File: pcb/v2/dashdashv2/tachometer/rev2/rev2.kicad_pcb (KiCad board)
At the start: 2 copper layers, 113 parts, among them Q1 BSS138, Q2 BSS138, Q3 BSS138, Q4 BSS138, Q5 BSS138

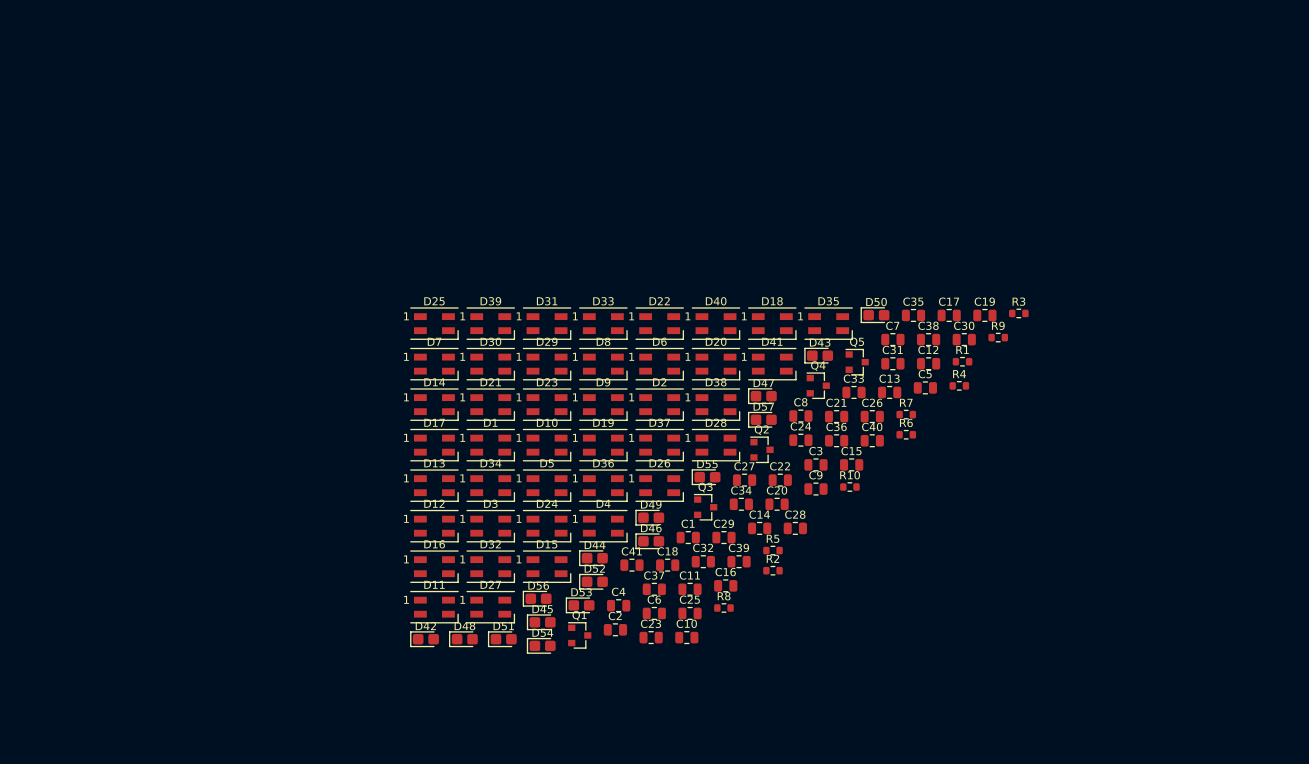
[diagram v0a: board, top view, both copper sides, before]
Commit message: tachometer, add neopixels
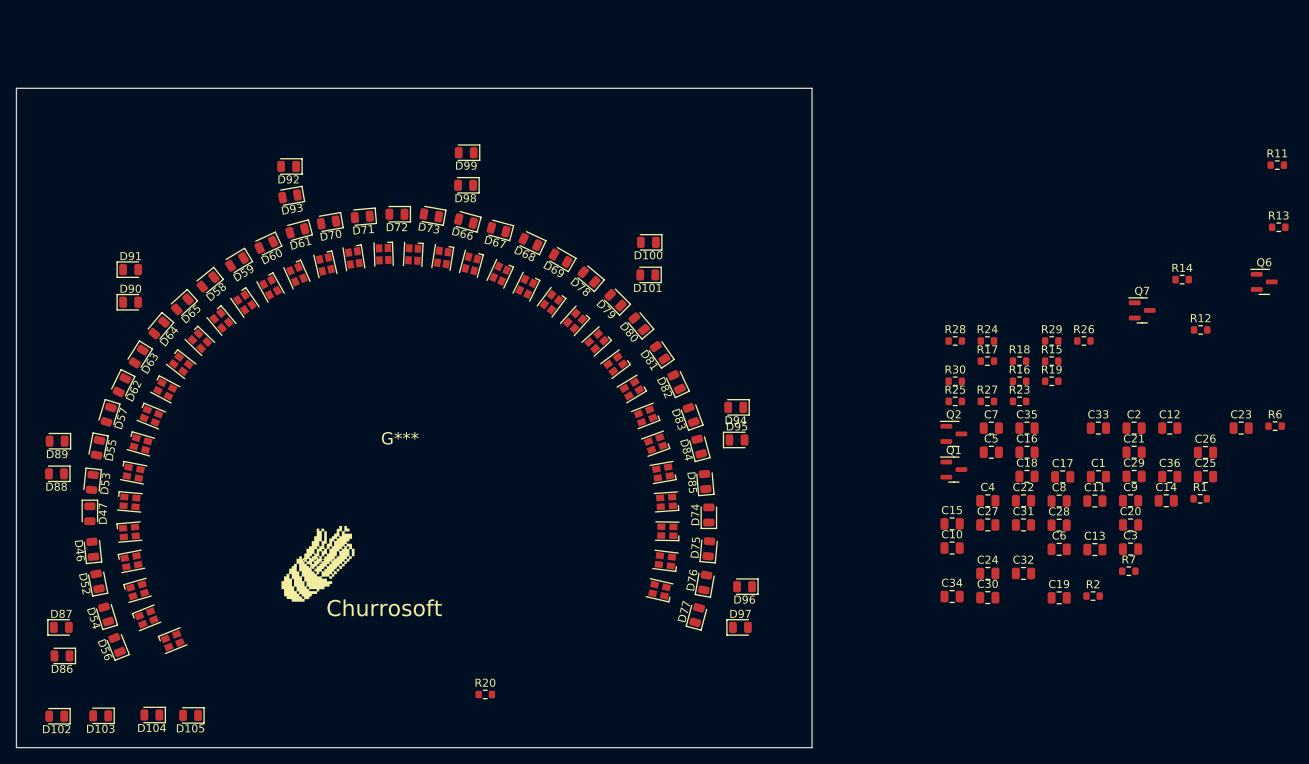
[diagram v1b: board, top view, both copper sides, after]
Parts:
- removed C37, C38, C39, C40, C41: 100nF, Capacitor_SMD:C_0805_2012Metric
- removed D37, D38, D39, D40, D41: WS2812B, LED_SMD:LED_SK6812MINI_PLCC4_3.5x3.5mm_P1.75mm
- removed D42, D43, D44, D45, D48, D49, D50, D51: LED, LED_SMD:LED_0805_2012Metric_Castellated
- removed Q3, Q4, Q5: BSS138, Package_TO_SOT_SMD:SOT-23
- removed R10, R3, R4, R5, R8, R9: 1k 1/10W +-1%, Resistor_SMD:R_0603_1608Metric
- added D100: LED, LED_SMD:LED_0805_2012Metric, F.Cu at (148.8, 78.1)
- added D101: LED, LED_SMD:LED_0805_2012Metric, F.Cu at (148.7, 82.2)
- added D102: LED, LED_SMD:LED_0805_2012Metric, F.Cu at (75.1, 137.2)
- added D103: LED, LED_SMD:LED_0805_2012Metric, F.Cu at (80.5, 137.2)
- added D104: LED, LED_SMD:LED_0805_2012Metric, F.Cu at (86.9, 137.1)
- added D105: LED, LED_SMD:LED_0805_2012Metric, F.Cu at (91.7, 137.1)
- added D58: LED, LED_SMD:LED_0805_2012Metric, F.Cu at (93.9, 83.1)
- added D59: LED, LED_SMD:LED_0805_2012Metric, F.Cu at (97.5, 80.6)
- added D60: LED, LED_SMD:LED_0805_2012Metric, F.Cu at (101.2, 78.4)
- added D61: LED, LED_SMD:LED_0805_2012Metric, F.Cu at (105.1, 76.7)
- added D62: LED, LED_SMD:LED_0805_2012Metric, F.Cu at (83.2, 95.9)
- added D63: LED, LED_SMD:LED_0805_2012Metric, F.Cu at (85.3, 92.4)
- added D64: LED, LED_SMD:LED_0805_2012Metric, F.Cu at (87.8, 88.8)
- added D65: LED, LED_SMD:LED_0805_2012Metric, F.Cu at (90.7, 85.9)
- added D66: LED, LED_SMD:LED_0805_2012Metric, F.Cu at (126.1, 75.5)
- added D67: LED, LED_SMD:LED_0805_2012Metric, F.Cu at (130.1, 76.6)
- added D68: LED, LED_SMD:LED_0805_2012Metric, F.Cu at (134.1, 78.1)
- added D69: LED, LED_SMD:LED_0805_2012Metric, F.Cu at (137.9, 80.1)
- added D70: LED, LED_SMD:LED_0805_2012Metric, F.Cu at (109.0, 75.7)
- added D71: LED, LED_SMD:LED_0805_2012Metric, F.Cu at (113.2, 75.0)
- added D72: LED, LED_SMD:LED_0805_2012Metric, F.Cu at (117.5, 74.6)
- added D73: LED, LED_SMD:LED_0805_2012Metric, F.Cu at (121.8, 74.8)
- added D74: LED, LED_SMD:LED_0805_2012Metric, F.Cu at (156.4, 112.1)
- added D75: LED, LED_SMD:LED_0805_2012Metric, F.Cu at (156.4, 116.3)
- added D76: LED, LED_SMD:LED_0805_2012Metric, F.Cu at (155.9, 120.5)
- added D77: LED, LED_SMD:LED_0805_2012Metric, F.Cu at (154.9, 124.6)
- added D78: LED, LED_SMD:LED_0805_2012Metric, F.Cu at (141.4, 82.5)
- added D79: LED, LED_SMD:LED_0805_2012Metric, F.Cu at (144.7, 85.3)
- added D80: LED, LED_SMD:LED_0805_2012Metric, F.Cu at (147.7, 88.3)
- added D81: LED, LED_SMD:LED_0805_2012Metric, F.Cu at (150.3, 91.9)
- added D82: LED, LED_SMD:LED_0805_2012Metric, F.Cu at (152.3, 95.6)
- added D83: LED, LED_SMD:LED_0805_2012Metric, F.Cu at (154.2, 99.7)
- added D84: LED, LED_SMD:LED_0805_2012Metric, F.Cu at (155.2, 103.6)
- added D85: LED, LED_SMD:LED_0805_2012Metric, F.Cu at (155.9, 108.0)
- added D86: LED, LED_SMD:LED_0805_2012Metric, F.Cu at (75.7, 129.7)
- added D87: LED, LED_SMD:LED_0805_2012Metric, F.Cu at (75.6, 126.1)
- added D88: LED, LED_SMD:LED_0805_2012Metric, F.Cu at (75.0, 107.0)
- added D89: LED, LED_SMD:LED_0805_2012Metric, F.Cu at (75.1, 102.9)
- added D90: LED, LED_SMD:LED_0805_2012Metric, F.Cu at (84.3, 85.6)
- added D91: LED, LED_SMD:LED_0805_2012Metric, F.Cu at (84.3, 81.5)
- added D92: LED, LED_SMD:LED_0805_2012Metric, F.Cu at (104.0, 68.7)
- added D93: LED, LED_SMD:LED_0805_2012Metric, F.Cu at (104.1, 72.4)
- added D94: LED, LED_SMD:LED_0805_2012Metric, F.Cu at (159.7, 98.7)
- added D95: LED, LED_SMD:LED_0805_2012Metric, F.Cu at (159.9, 102.8)
- added D96: LED, LED_SMD:LED_0805_2012Metric, F.Cu at (160.8, 121.1)
- added D97: LED, LED_SMD:LED_0805_2012Metric, F.Cu at (160.3, 126.1)
- added D98: LED, LED_SMD:LED_0805_2012Metric, F.Cu at (126.0, 71.0)
- added D99: LED, LED_SMD:LED_0805_2012Metric, F.Cu at (126.1, 67.0)
- added G***: LOGO, LOGO, F.Cu at (117.9, 102.6)
- added G***: LOGO, LOGO, F.Cu at (107.8, 118.2)
- added Q6: BSS138, Package_TO_SOT_SMD:SOT-23, F.Cu at (225.6, 83.1)
- added Q7: BSS138, Package_TO_SOT_SMD:SOT-23, F.Cu at (210.4, 86.6)
- added R11: 1k 1/10W +-1%, Resistor_SMD:R_0603_1608Metric, F.Cu at (227.2, 68.5)
- added R12: 1k 1/10W +-1%, Resistor_SMD:R_0603_1608Metric, F.Cu at (217.7, 89.1)
- added R13: 1k 1/10W +-1%, Resistor_SMD:R_0603_1608Metric, F.Cu at (227.4, 76.3)
- added R14: 1k 1/10W +-1%, Resistor_SMD:R_0603_1608Metric, F.Cu at (215.4, 82.8)
- added R15: 1k 1/10W +-1%, Resistor_SMD:R_0603_1608Metric, F.Cu at (199.1, 92.9)
- added R16: 1k 1/10W +-1%, Resistor_SMD:R_0603_1608Metric, F.Cu at (195.1, 95.4)
- added R17: 1k 1/10W +-1%, Resistor_SMD:R_0603_1608Metric, F.Cu at (191.1, 92.9)
- added R18: 1k 1/10W +-1%, Resistor_SMD:R_0603_1608Metric, F.Cu at (195.1, 92.9)
- added R19: 1k 1/10W +-1%, Resistor_SMD:R_0603_1608Metric, F.Cu at (199.1, 95.4)
- added R20: 1k 1/10W +-1%, Resistor_SMD:R_0603_1608Metric, F.Cu at (128.5, 134.5)
- added R23: 1k 1/10W +-1%, Resistor_SMD:R_0603_1608Metric, F.Cu at (195.1, 98.0)
- added R24: 1k 1/10W +-1%, Resistor_SMD:R_0603_1608Metric, F.Cu at (191.1, 90.4)
- added R25: 1k 1/10W +-1%, Resistor_SMD:R_0603_1608Metric, F.Cu at (187.1, 98.0)
- added R26: 1k 1/10W +-1%, Resistor_SMD:R_0603_1608Metric, F.Cu at (203.1, 90.4)
- added R27: 1k 1/10W +-1%, Resistor_SMD:R_0603_1608Metric, F.Cu at (191.1, 98.0)
- added R28: 1k 1/10W +-1%, Resistor_SMD:R_0603_1608Metric, F.Cu at (187.1, 90.4)
- added R29: 1k 1/10W +-1%, Resistor_SMD:R_0603_1608Metric, F.Cu at (199.1, 90.4)
- added R30: 1k 1/10W +-1%, Resistor_SMD:R_0603_1608Metric, F.Cu at (187.1, 95.4)
- D1, D10, D11, D12, D13, D14, D15, D16, D17, D18, D19, D2, D20, D21, D22, D23, D24, D25, D26, D27, D28, D29, D3, D30, D31, D32, D33, D34, D35, D36, D4, D5, D6, D7, D8, D9: footprint LED_SMD:LED_SK6812MINI_PLCC4_3.5x3.5mm_P1.75mm -> LED_SMD:LED_Cree-PLCC4_2x2mm_CW
- D46, D47, D52, D53, D54, D55, D56, D57: footprint LED_SMD:LED_0805_2012Metric_Castellated -> LED_SMD:LED_0805_2012Metric
- moved D47 85.3 mm to (79.2, 112.0), turned to -90 degrees
- moved D57 81.7 mm to (81.5, 99.6), turned to -107 degrees
- moved C23 78.1 mm to (222.7, 101.3)
- moved D55 76.1 mm to (80.2, 103.7), turned to -101 degrees
- moved D46 69.6 mm to (79.5, 116.4), turned to 96 degrees
- moved C2 69.4 mm to (209.4, 101.3)
- moved D2 69.3 mm to (86.3, 124.9), turned to 22 degrees
- moved D6 68.2 mm to (84.2, 110.5), turned to -5 degrees
- moved C25 66.5 mm to (218.3, 107.3)
- moved D53 62.9 mm to (79.5, 108.1), turned to -96 degrees
- moved D52 62.0 mm to (80.2, 120.4), turned to 101 degrees
- moved D4 59.0 mm to (84.4, 117.9), turned to 11 degrees
- moved D8 58.5 mm to (85.6, 103.3), turned to -16 degrees
- moved D9 56.4 mm to (86.9, 99.8), turned to -22 degrees
- moved D54 54.5 mm to (81.2, 124.5), turned to 107 degrees
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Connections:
- D56 pad 1: /BA_1 -> Net-(D56-Pad1)
- D57 pad 1: /BA_2 -> Net-(D57-Pad1)
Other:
- board outline added: 99.2 x 82.2 mm
- board text added: "Churrosoft"

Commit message: routing neopixel
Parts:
- moved D1 1.91 mm to (87.8, 128.5)
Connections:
- C27 pad 2: Net-(C27-Pad2) -> +5VA
- C28 pad 2: Net-(C27-Pad2) -> +5VA
- C29 pad 2: Net-(C27-Pad2) -> +5VA
- C30 pad 2: Net-(C27-Pad2) -> +5VA
- C31 pad 2: Net-(C27-Pad2) -> +5VA
- D27 pad 1: Net-(C27-Pad2) -> +5VA
- D28 pad 1: Net-(C27-Pad2) -> +5VA
- D29 pad 1: Net-(C27-Pad2) -> +5VA
- D30 pad 1: Net-(C27-Pad2) -> +5VA
- D31 pad 1: Net-(C27-Pad2) -> +5VA
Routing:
- net Net-(D16-Pad2): track 0.00 -> 3.78 mm
- net Net-(D17-Pad2): track 0.00 -> 3.74 mm
- net Net-(D10-Pad2): track 0.00 -> 3.72 mm
- net Net-(D18-Pad2): track 0.00 -> 3.72 mm
- net Net-(D12-Pad2): track 0.00 -> 3.67 mm
- net Net-(D11-Pad2): track 0.00 -> 3.66 mm
- net Net-(D23-Pad2): track 0.00 -> 3.62 mm
- net Net-(D15-Pad2): track 0.00 -> 3.58 mm
- net Net-(D10-Pad4): track 0.00 -> 3.49 mm
- net Net-(D4-Pad2): track 0.00 -> 3.45 mm
- net Net-(D29-Pad2): track 0.00 -> 3.41 mm
- net Net-(D3-Pad2): track 0.00 -> 3.39 mm
- net Net-(D8-Pad2): track 0.00 -> 3.35 mm
- net Net-(D22-Pad2): track 0.00 -> 3.29 mm
- net Net-(D1-Pad2): track 0.00 -> 3.27 mm
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
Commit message: tach v2, routing & 3D
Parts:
- removed R12, R13, R2, R6: 1k 1/10W +-1%, Resistor_SMD:R_0603_1608Metric
- added C37: 100nF, Capacitor_SMD:C_0805_2012Metric, B.Cu at (169.7, 73.8)
- added C38: 100nF, Capacitor_SMD:C_0805_2012Metric, B.Cu at (172.2, 76.4)
- added C39: 100nF, Capacitor_SMD:C_0805_2012Metric, B.Cu at (174.6, 79.2)
- added C40: 100nF, Capacitor_SMD:C_0805_2012Metric, B.Cu at (176.6, 82.6)
- added C41: 100nF, Capacitor_SMD:C_0805_2012Metric, B.Cu at (178.3, 85.9)
- added C42: 100nF, Capacitor_SMD:C_0805_2012Metric, B.Cu at (179.5, 89.4)
- added C43: 100nF, Capacitor_SMD:C_0805_2012Metric, B.Cu at (180.4, 92.9)
- added C44: 100nF, Capacitor_SMD:C_0805_2012Metric, B.Cu at (180.7, 96.4)
- added C45: 100nF, Capacitor_SMD:C_0805_2012Metric, B.Cu at (180.8, 100.2)
- added C46: 100nF, Capacitor_SMD:C_0805_2012Metric, B.Cu at (180.5, 103.8)
- added C47: 100nF, Capacitor_SMD:C_0805_2012Metric, B.Cu at (179.7, 107.6)
- added C53: 100nF, Capacitor_SMD:C_0603_1608Metric, B.Cu at (155.3, 106.8)
- added C54: 30pF, Capacitor_SMD:C_0603_1608Metric, B.Cu at (136.7, 95.1)
- added C55: 30pF, Capacitor_SMD:C_0603_1608Metric, B.Cu at (136.7, 87.8)
- added C56: 100nF, Capacitor_SMD:C_0603_1608Metric, B.Cu at (162.7, 113.4)
- added C57: 30pF, Capacitor_SMD:C_0603_1608Metric, B.Cu at (161.4, 117.0)
- added C58: 2.2uF, Capacitor_SMD:C_0603_1608Metric, B.Cu at (147.1, 98.4)
- added D106: GREEN, LED_SMD:LED_0603_1608Metric, B.Cu at (192.4, 68.5)
- added D107: BLUE, LED_SMD:LED_0603_1608Metric, B.Cu at (189.9, 74.0)
- added D108: RED, LED_SMD:LED_0603_1608Metric, B.Cu at (185.6, 72.2)
- added D111: WS2812B, LED_SMD:LED_Cree-PLCC4_2x2mm_CW, F.Cu at (119.5, 109.3)
- added D112: WS2812B, LED_SMD:LED_Cree-PLCC4_2x2mm_CW, F.Cu at (118.5, 106.3)
- added D113: WS2812B, LED_SMD:LED_Cree-PLCC4_2x2mm_CW, F.Cu at (117.9, 103.0)
- added D114: WS2812B, LED_SMD:LED_Cree-PLCC4_2x2mm_CW, F.Cu at (117.7, 99.7)
- added D115: WS2812B, LED_SMD:LED_Cree-PLCC4_2x2mm_CW, F.Cu at (117.8, 96.5)
- added H1: MountingHole, MountingHole:MountingHole_2.2mm_M2_Pad, F.Cu at (110.0, 60.0)
- added H10: USB+, TestPoint:TestPoint_Pad_D1.5mm, B.Cu at (152.8, 76.8)
- added H11: USB_GND, TestPoint:TestPoint_Pad_D1.5mm, B.Cu at (167.0, 88.3)
- added H2: MountingHole, MountingHole:MountingHole_2.2mm_M2_Pad, F.Cu at (125.0, 115.0)
- added H3: MountingHole, MountingHole:MountingHole_2.2mm_M2_Pad, F.Cu at (165.3, 82.4)
- added H4: MountingHole, MountingHole:MountingHole_2.2mm_M2_Pad, F.Cu at (169.2, 61.1)
- added H5: MountingHole, MountingHole:MountingHole_2.2mm_M2_Pad, F.Cu at (131.1, 61.6)
- added H6: MountingHole, MountingHole:MountingHole_2.2mm_M2_Pad, F.Cu at (185.0, 60.0)
- added H7: MountingHole, MountingHole:MountingHole_2.2mm_M2_Pad, F.Cu at (180.0, 115.0)
- added H8: MountingHole, MountingHole:MountingHole_2.2mm_M2_Pad, F.Cu at (133.0, 80.0)
- added H9: USB-, TestPoint:TestPoint_Pad_D1.5mm, B.Cu at (158.7, 77.3)
- added J1: Tag connect, Connector:Tag-Connect_TC2030-IDC-FP_2x03_P1.27mm_Vertical, B.Cu at (159.1, 89.0)
- added J2: RPM_CONN1, Connector_PinHeader_1.27mm:PinHeader_2x05_P1.27mm_Vertical, B.Cu at (126.9, 94.5)
- added JP1: BOOTSEL, Jumper:SolderJumper-2_P1.3mm_Open_TrianglePad1.0x1.5mm, B.Cu at (142.2, 79.1)
- added R21: 10k, Resistor_SMD:R_0603_1608Metric, B.Cu at (151.3, 83.0)
- added R22: 1k, Resistor_SMD:R_0603_1608Metric, B.Cu at (140.7, 82.4)
- added R31: 1k, Resistor_SMD:R_0603_1608Metric, B.Cu at (189.2, 68.4)
- added R32: 27R, Resistor_SMD:R_0603_1608Metric, B.Cu at (153.8, 80.1)
- added R33: 27R, Resistor_SMD:R_0603_1608Metric, B.Cu at (157.0, 80.6)
- added R34: 1k, Resistor_SMD:R_0603_1608Metric, B.Cu at (193.6, 73.2)
- added R35: 1k, Resistor_SMD:R_0603_1608Metric, B.Cu at (185.9, 67.9)
- added U1: W25Q128JVS, Package_SO:SOIC-8_5.23x5.23mm_P1.27mm, B.Cu at (146.5, 78.0)
- added U2: LP5907MFX-3.3, Package_TO_SOT_SMD:SOT-23-5, B.Cu at (131.0, 110.5)
- added U3: SRV05-4, Package_TO_SOT_SMD:SOT-23-6, B.Cu at (133.4, 97.5)
- added U4: RP2040, Package_DFN_QFN:QFN-56-1EP_7x7mm_P0.4mm_EP3.2x3.2mm, B.Cu at (146.1, 92.0)
- added U6: YAAJ_DCDC_StepDown_LM2596, dashdash_lib:YAAJ_DCDC_StepDown_LM2596, B.Cu at (171.2, 105.7)
- added Y1: 12MHz, Crystal:Crystal_SMD_3225-4Pin_3.2x2.5mm, B.Cu at (136.6, 91.6)
- C1: value 100nF -> 2.2uF; footprint Capacitor_SMD:C_0805_2012Metric -> Capacitor_SMD:C_0603_1608Metric; moved to B.Cu
- C10, C11, C2, C3, C4, C5, C6, C7, C8, C9: footprint Capacitor_SMD:C_0805_2012Metric -> Capacitor_SMD:C_0603_1608Metric; moved to B.Cu
- C12, C13, C14, C15, C16, C17, C18, C19, C20, C21, C22, C23, C24, C25, C26, C27, C28, C29, C30, C31, C32, C33, C34, C35, C36, Q1, Q2, Q6, Q7, R1, R11, R14, R15, R16, R17, R18, R19, R20, R23, R24, R25, R26, R27, R28, R29, R30, R7: moved to B.Cu
- moved R7 103.7 mm to (115.2, 74.5)
- moved C23 102.9 mm to (122.9, 76.1), turned to 130 degrees
- moved C14 98.4 mm to (115.0, 107.2), turned to -170 degrees
- moved C12 97.1 mm to (117.6, 114.0), turned to -160 degrees
- moved C25 96.7 mm to (128.5, 71.3), turned to 110 degrees
- moved C20 96.4 mm to (116.6, 85.5), turned to 160 degrees
- moved C21 93.7 mm to (118.3, 82.1), turned to 150 degrees
- moved C26 93.4 mm to (131.6, 69.5), turned to 100 degrees
- moved C19 91.0 mm to (115.4, 89.0), turned to 160 degrees
- moved R16 90.5 mm to (105.0, 86.5), turned to 180 degrees
- moved R29 90.5 mm to (109.3, 101.9), turned to -90 degrees
- moved R1 90.0 mm to (144.6, 57.6), turned to 90 degrees
- moved C13 88.6 mm to (116.1, 110.6), turned to -160 degrees
- moved C17 87.1 mm to (114.1, 96.2), turned to 170 degrees
- moved C18 82.8 mm to (114.6, 92.5), turned to 160 degrees
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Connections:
- net +12V renamed +12LF
- net /DIN renamed /TACH_DIN
- C1 pad 2: +5VA -> +3V3
- C10 pad 1: GND -> +1V1
- C10 pad 2: +5VA -> GND
- C11 pad 1: GND -> +1V1
- C11 pad 2: +5VA -> GND
- C2 pad 1: GND -> +3V3
- C2 pad 2: +5VA -> GND
- C3 pad 1: GND -> +3V3
- C3 pad 2: +5VA -> GND
- C4 pad 1: GND -> +3V3
- C4 pad 2: +5VA -> GND
- C5 pad 1: GND -> +3V3
- C5 pad 2: +5VA -> GND
- C6 pad 1: GND -> +3V3
- C6 pad 2: +5VA -> GND
- C7 pad 1: GND -> +3V3
- C7 pad 2: +5VA -> GND
- C8 pad 1: GND -> +3V3
- C8 pad 2: +5VA -> GND
- C9 pad 1: GND -> VDDA
- C9 pad 2: +5VA -> GND
- Q1 pad 3: Net-(Q1-Pad3) -> /BA_1
- Q2 pad 3: Net-(Q2-Pad3) -> /BA_2
- Q6 pad 3: Net-(Q6-Pad3) -> /BA_4
- Q7 pad 3: Net-(Q7-Pad3) -> /BA_3
- R1 pad 1: /BA_1 -> Net-(Q1-Pad1)
- R1 pad 2: Net-(Q1-Pad3) -> PWM_BACK_RPM
- R11 pad 2: /BA_4_L -> PWM_BACK_RPM
- R14 pad 2: /BA_3_L -> PWM_BACK_RPM
- R7 pad 2: /BA_2_L -> PWM_BACK_RPM
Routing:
- net +12LF: track 0.00 -> 37.6 mm, vias 0 -> 9
- net Net-(D103-Pad1): track 0.00 -> 4.54 mm
- net Net-(D1-Pad2): track 3.27 -> 6.95 mm
- net Net-(D102-Pad1): track 0.00 -> 3.63 mm
- net Net-(D86-Pad1): track 0.00 -> 3.59 mm
- net Net-(D104-Pad1): track 0.00 -> 2.97 mm
- net Net-(D82-Pad1): track 0.00 -> 2.75 mm
- net Net-(D112-Pad2): track 0.00 -> 2.70 mm
- net Net-(D80-Pad1): track 0.00 -> 2.69 mm
- net Net-(D114-Pad2): track 0.00 -> 2.68 mm
- net Net-(D84-Pad1): track 0.00 -> 2.66 mm
- net Net-(D58-Pad1): track 0.00 -> 2.62 mm
- net Net-(D63-Pad1): track 0.00 -> 2.60 mm
- net Net-(D111-Pad2): track 0.00 -> 2.59 mm
- net Net-(D78-Pad1): track 0.00 -> 2.58 mm
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- added copper zone on In1.Cu, net +12LF
- added copper zone on In1.Cu, net +5VA
- added copper zone on B.Cu, net GND
- added copper zone on F.Cu, net GND
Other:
- board size 99.2 x 82.2 mm -> 95 x 77 mm
- copper layers 2 -> 4

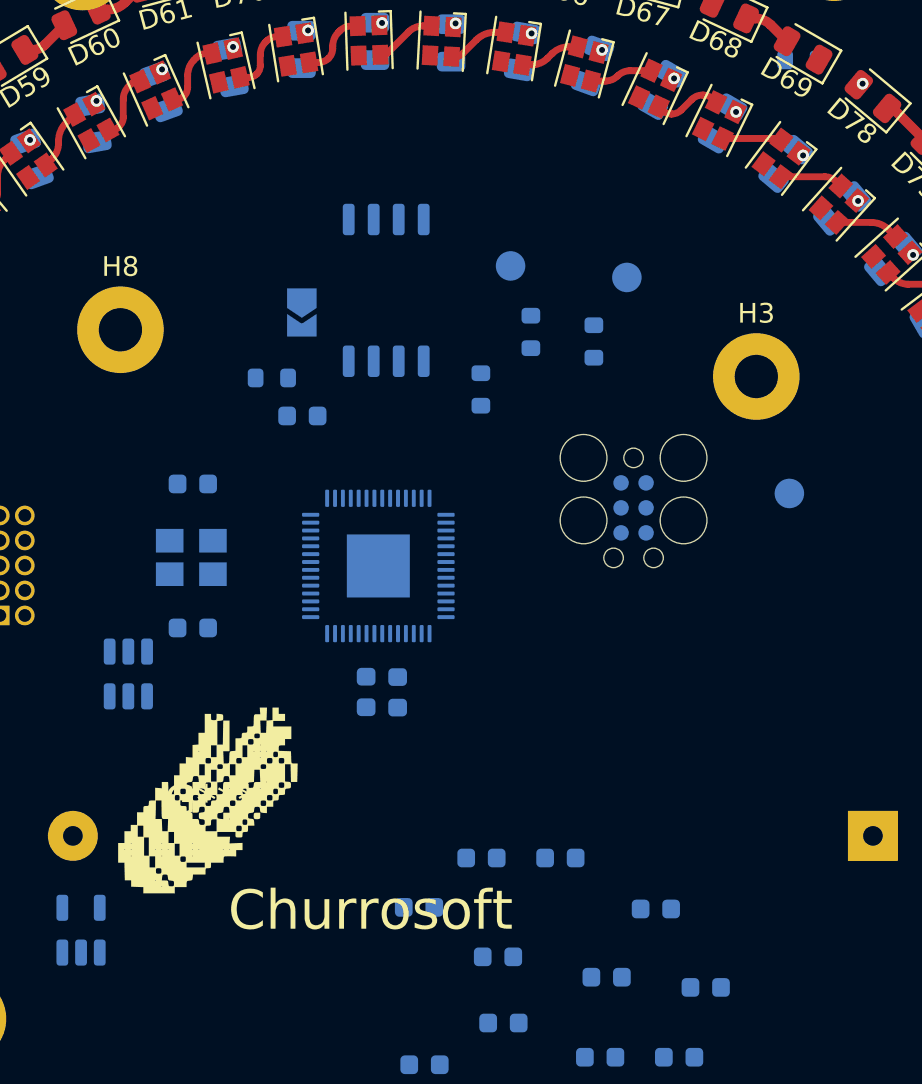
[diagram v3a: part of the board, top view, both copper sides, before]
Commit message: routing spi flash
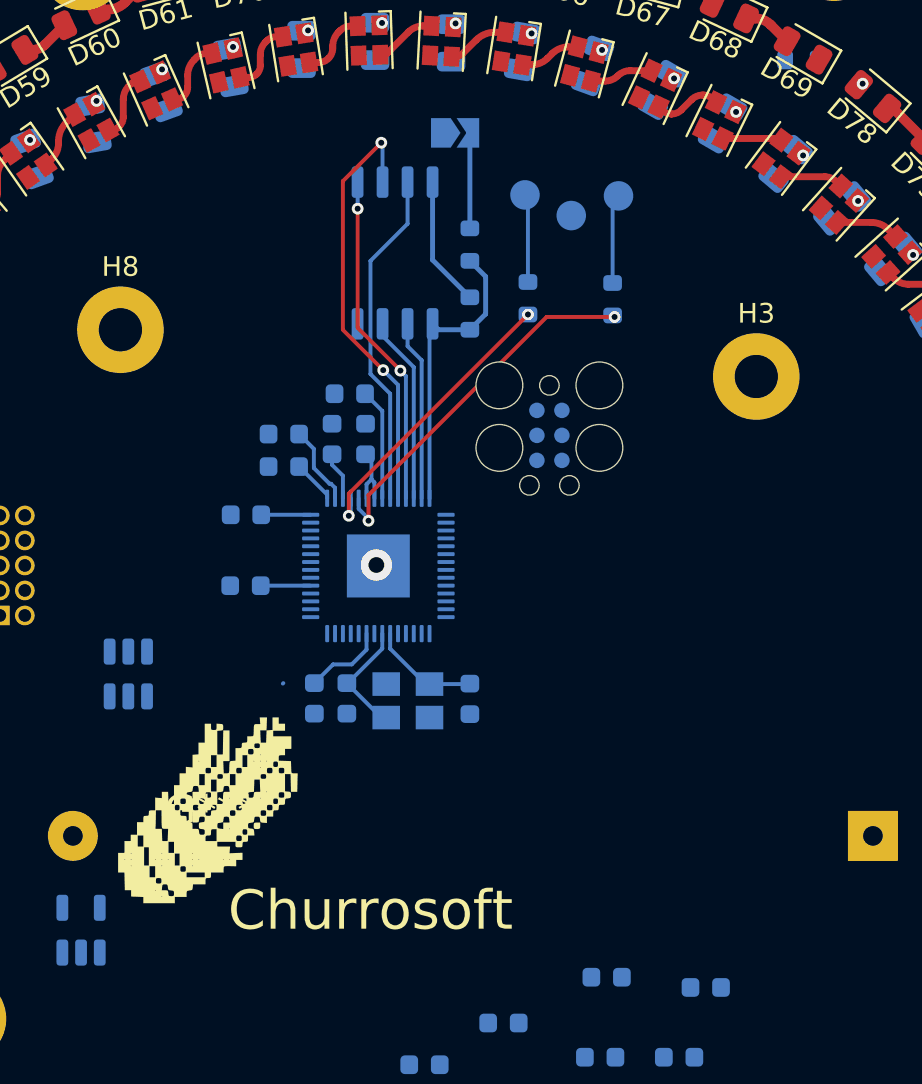
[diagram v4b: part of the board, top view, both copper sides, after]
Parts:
- moved C9 29.4 mm to (141.3, 87.0)
- moved C4 27.1 mm to (145.4, 85.5), turned to 90 degrees
- moved C8 23.8 mm to (141.3, 85.3)
- moved C53 23.6 mm to (139.4, 89.4), turned to 0 degrees
- moved C3 18.6 mm to (139.3, 93.0)
- moved H11 17.9 mm to (155.9, 74.2)
- moved C10 15.2 mm to (144.7, 83.2), turned to 180 degrees
- moved C54 14.5 mm to (150.8, 98.8), turned to 90 degrees
- moved C55 13.4 mm to (144.5, 98.7), turned to 90 degrees
- moved Y1 13.2 mm to (147.6, 98.8), turned to 0 degrees
- moved R22 12.1 mm to (150.8, 75.7), turned to 90 degrees
- moved JP1 12.0 mm to (150.0, 70.0), turned to 0 degrees
- moved H9 6.66 mm to (153.6, 73.2)
- moved H10 6.54 mm to (158.3, 73.2)
- moved J1 5.64 mm to (154.8, 85.4)
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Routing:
- net /QSPI_SCLK: track 0.00 -> 22.1 mm, vias 0 -> 2
- net +3V3: track 0.00 -> 19.2 mm
- net /D-: track 0.00 -> 19.0 mm, vias 0 -> 2
- net /QSPI_SD3: track 0.00 -> 17.3 mm
- net /QSPI_SD0: track 0.00 -> 17.1 mm, vias 0 -> 2
- net /QSPI_SS: track 0.00 -> 15.1 mm
- net /D+: track 0.00 -> 14.9 mm, vias 0 -> 2
- net +1V1: track 0.00 -> 12.5 mm
- net /QSPI_SD2: track 0.00 -> 9.52 mm
- net /QSPI_SD1: track 0.00 -> 9.16 mm
- net /xout: track 0.00 -> 6.01 mm
- net /xin: track 0.00 -> 5.57 mm
- net Net-(JP1-Pad2): track 0.00 -> 4.86 mm
- net /USB_D+: track 0.00 -> 4.55 mm
- net /USB_D-: track 0.00 -> 4.49 mm
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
